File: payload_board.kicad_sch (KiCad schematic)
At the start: 93 parts, among them IC1 RP2040_QFN56, IC2 AZ1117CH-3.3TRG1, J1 Cam_PicoLock, J11 Stemma, J12 5025700893, J15 Debug_Conn, J2 Cam_Conn, J3 Antenna_Conn, J4 usb jumper, J5 Display_Conn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

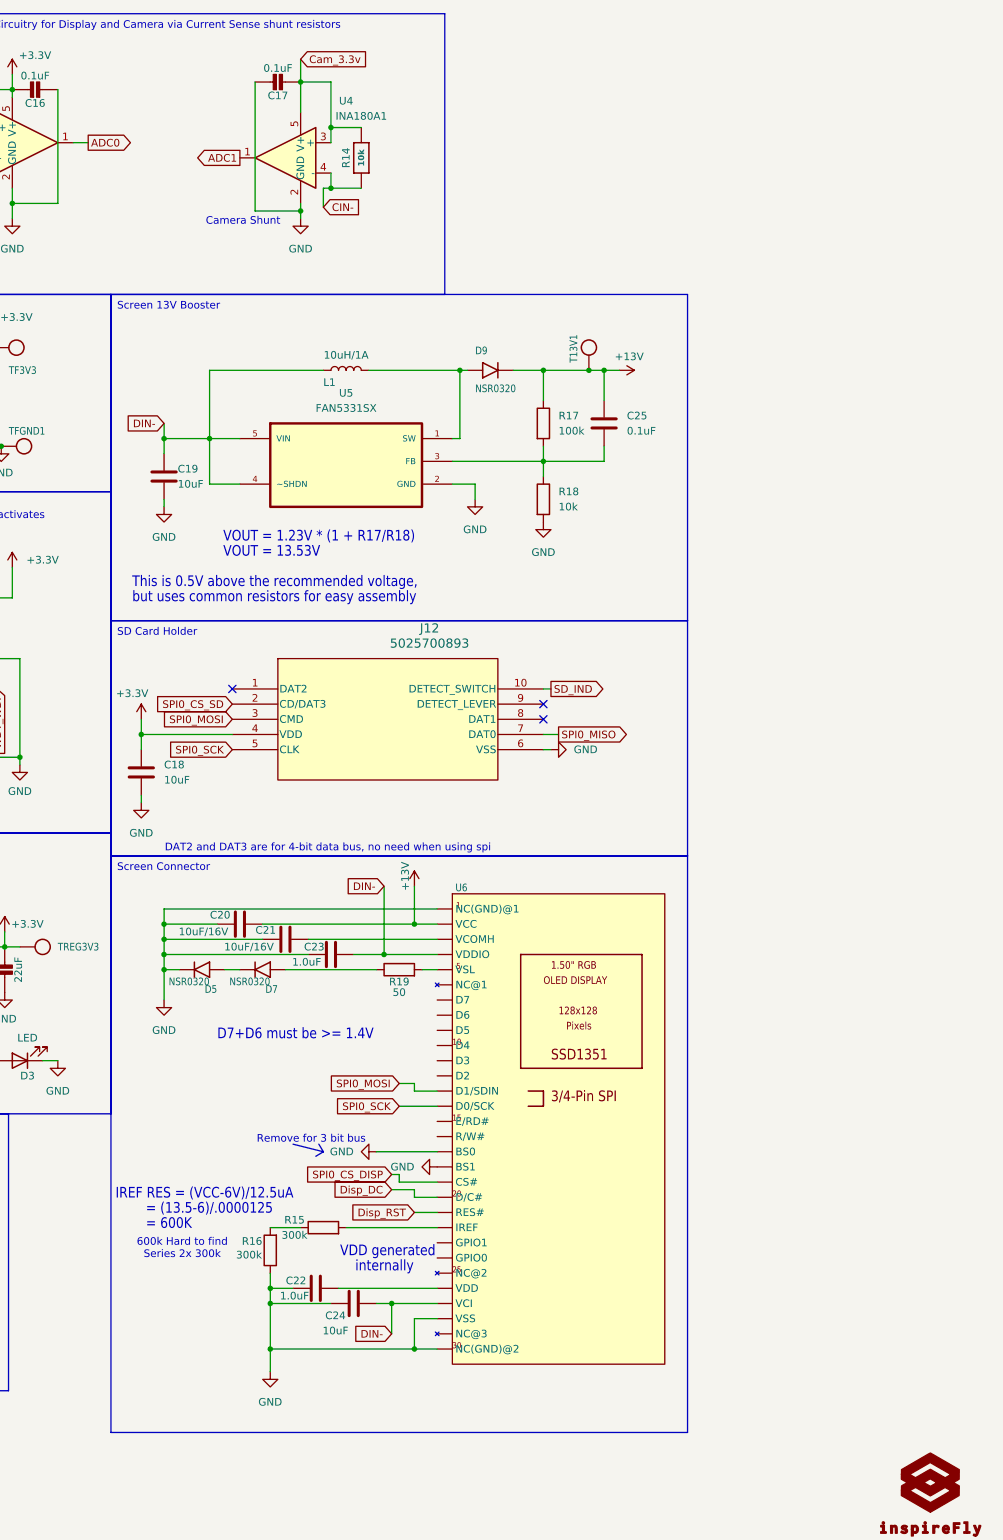
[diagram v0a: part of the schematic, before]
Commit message: Fixed RP2040 connections and changed sd card
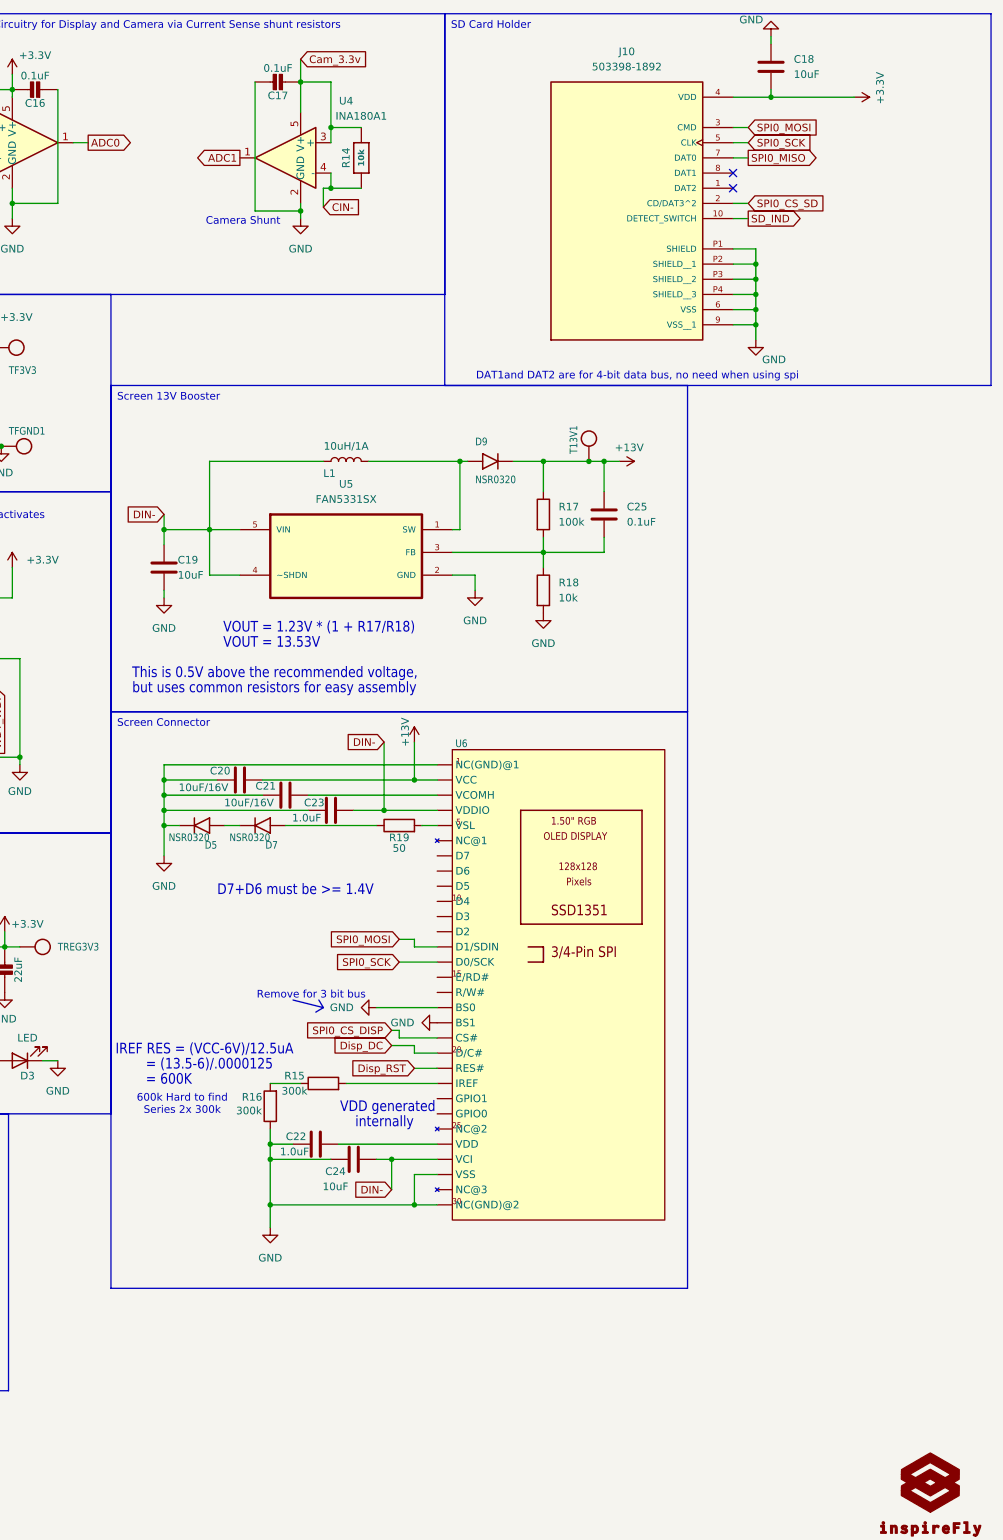
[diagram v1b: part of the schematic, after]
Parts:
- removed J12: 5025700893, PayloadBoard:502570-0893_MOL, symbol PayloadBoard:5025700893
- added J10: 503398-1892, PayloadBoard:MOLEX_503398-1892, symbol PayloadBoard:503398-1892
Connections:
- net +3.3V: now also C18.2, J10.4 (VDD); no longer C18.1
- net GND: now also C18.1, J10.6 (VSS), J10.9 (VSS__1), J10.P1 (SHIELD), J10.P2 (SHIELD__1), J10.P3 (SHIELD__2), J10.P4 (SHIELD__3); no longer C18.2
- net SD_IND: now also J10.10 (DETECT_SWITCH)
- net SPI0_CS_SD: now also J10.2 (CD/DAT3^2)
- net SPI0_MISO: now also J10.7 (DAT0)
- net SPI0_MOSI: now also J10.3 (CMD)
- net SPI0_SCK: now also J10.5 (CLK)
- no-connect marks 9 -> 8
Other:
- note added: "DAT1and DAT2 are for 4-bit data bus, no need when using spi"
- note removed: "DAT2 and DAT3 are for 4-bit data bus, no need when using spi"
- moved on the sheet: C18, C19, C20, C21, C22, C23, C24, C25, D5, D7, D9, L1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

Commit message: Changed some components to decrease bom count (C18, C25)
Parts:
- C18: footprint Capacitor_SMD:C_0603_1608Metric_Pad1.08x0.95mm_HandSolder -> Capacitor_SMD:C_1206_3216Metric_Pad1.33x1.80mm_HandSolder
- C25: footprint Capacitor_SMD:C_0603_1608Metric_Pad1.08x0.95mm_HandSolder -> Capacitor_SMD:C_0402_1005Metric_Pad0.74x0.62mm_HandSolder
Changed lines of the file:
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@@
 			)
 		)
-		(property "Footprint" "Capacitor_SMD:C_0603_1608Metric_Pad1.08x0.95mm_HandSolder"
+		(property "Footprint" "Capacitor_SMD:C_0402_1005Metric_Pad0.74x0.62mm_HandSolder"
 			(at 343.8652 100.33 0)
 			(effects
@@
 			)
 		)
-		(property "Footprint" "Capacitor_SMD:C_0603_1608Metric_Pad1.08x0.95mm_HandSolder"
+		(property "Footprint" "Capacitor_SMD:C_1206_3216Metric_Pad1.33x1.80mm_HandSolder"
 			(at 371.8052 25.4 0)
 			(effects

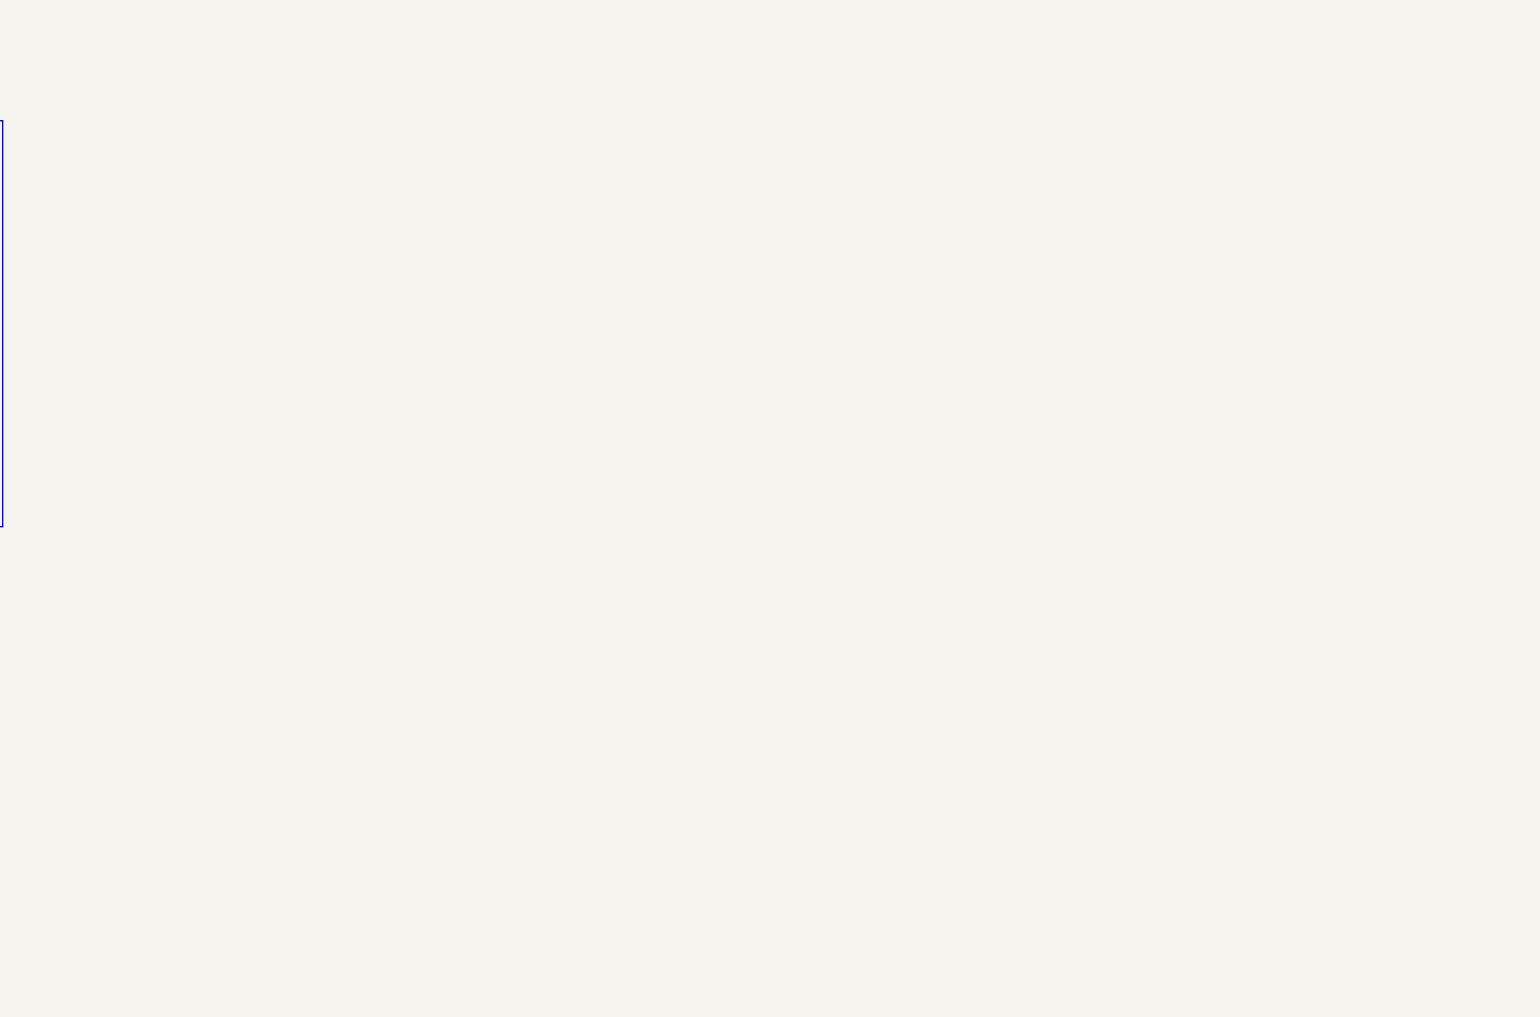
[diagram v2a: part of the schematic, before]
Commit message: stuck with new buck converter Trying to understand why BOOT is limited to 10 V, even if output is supposed to be 14V
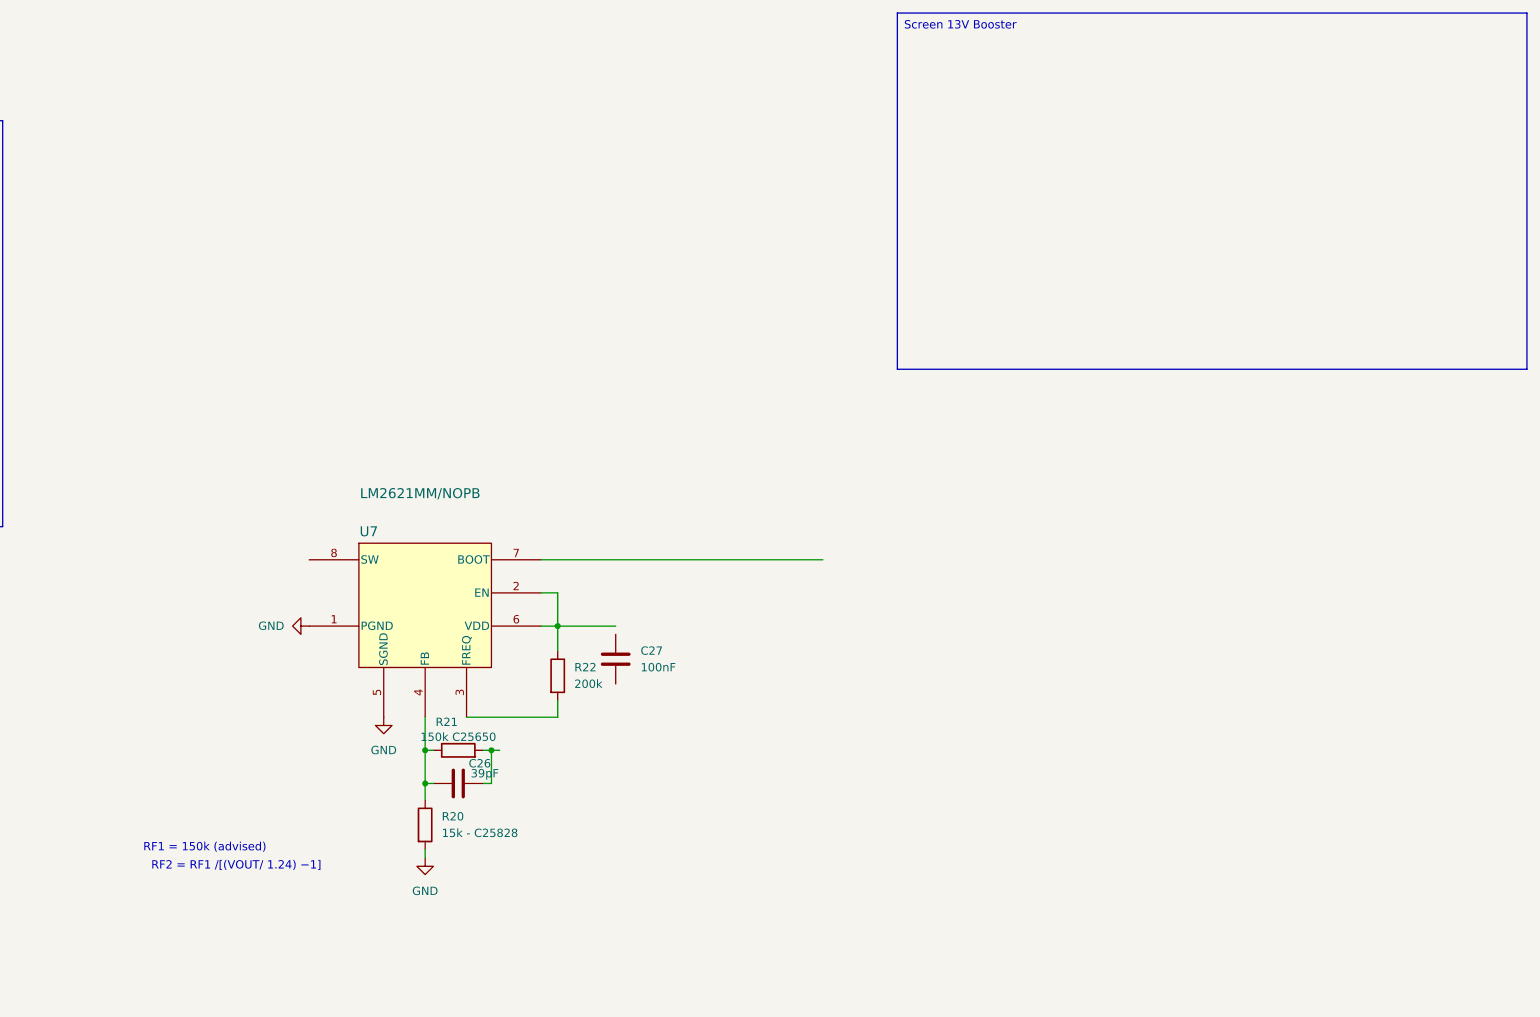
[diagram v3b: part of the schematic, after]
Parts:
- added C26: 39pF, symbol Device:C
- added C27: 100nF, symbol Device:C
- added R20: 15k - C25828, symbol Device:R
- added R21: 150k C25650, symbol Device:R
- added R22: 200k, symbol Device:R
- added U7: LM2621MM/NOPB, PayloadBoard:MUA08A, symbol PayloadBoard:LM2621MM_NOPB
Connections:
- net GND: now also R20.2, U7.1 (PGND), U7.5 (SGND)
- new net: C26.2, R20.1, R21.1, U7.4 (FB)
- new net: C26.1, R21.2
- new net: R22.1, U7.2 (EN), U7.6 (VDD)
- new net: R22.2, U7.3 (FREQ)
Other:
- note added: "RF1 = 150k (advised)"
- note added: "RF2 = RF1 /[(VOUT/ 1.24) −1]"

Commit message: Added new 13V boost converter
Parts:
- removed C25: 0.1uF, Capacitor_SMD:C_0402_1005Metric_Pad0.74x0.62mm_HandSolder, symbol Device:C
- removed C27: 100nF, symbol Device:C
- removed D9: NSR0320, Diode_SMD:D_SOD-323, symbol Adafruit ItsyBitsy RP2040-eagle-import:DIODESOD-323F
- removed R17: 100k, Resistor_SMD:R_0603_1608Metric_Pad0.98x0.95mm_HandSolder, symbol Device:R
- removed R18: 10k, Resistor_SMD:R_0603_1608Metric_Pad0.98x0.95mm_HandSolder, symbol Device:R
- removed R22: 200k, symbol Device:R
- removed U5: FAN5331SX, Package_TO_SOT_SMD:SOT-23-5_HandSoldering, symbol PayloadBoard:FAN5331SX
- removed U7: LM2621MM/NOPB, PayloadBoard:MUA08A, symbol PayloadBoard:LM2621MM_NOPB
- added U7: TLV61046ADB, Package_TO_SOT_SMD:SOT-23-6, symbol Regulator_Switching:TLV61046ADB
- C19: value 10uF -> 1uF; footprint Capacitor_SMD:C_0603_1608Metric_Pad1.08x0.95mm_HandSolder -> Capacitor_SMD:C_0402_1005Metric_Pad0.74x0.62mm_HandSolder
- C26: value 39pF -> 4.7uF; footprint (none) -> Resistor_SMD:R_0805_2012Metric_Pad1.20x1.40mm_HandSolder
- R20: value 15k - C25828 -> 16k; footprint (none) -> Resistor_SMD:R_0805_2012Metric_Pad1.20x1.40mm_HandSolder
- R21: value 150k C25650 -> 1k; footprint (none) -> Resistor_SMD:R_0402_1005Metric_Pad0.72x0.64mm_HandSolder
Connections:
- net +13V: now also C26.2, R20.1, U7.5 (VOUT)
- net DIN-: now also C19.2, U7.4 (EN), U7.6 (VI); no longer C19.1
- net GND: now also C19.1, C26.1, R21.2, U7.2 (GND); no longer C19.2, R20.2
- net at L1.2: now also U7.1 (SW)
- new net: R20.2, R21.1, U7.3 (FB)
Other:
- note added: "16k = (13.515/0.795-1)1k"
- note added: "R20 = (VOUT/0.795-1)R21"
- note removed: "RF1 = 150k (advised)"
- note removed: "RF2 = RF1 /[(VOUT/ 1.24) −1]"
- note removed: "VOUT = 1.23V * (1 + R17/R18)"
- note removed: "VOUT = 13.53V"
- moved on the sheet: C19, L1, T13V1

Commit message: Change part selection to reflect avaliability
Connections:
- net GND: now also IC1.40 (GPIO28/AD2), IC1.41 (GPIO29/AD3)
- no-connect marks 8 -> 7
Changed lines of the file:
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@@
 	)
 	(junction
+		(at 54.61 114.3)
+		(diameter 0)
+		(color 0 0 0 0)
+	)
+	(junction
 		(at 368.3 54.61)
 		(diameter 0)
@@
 	)
 	(no_connect
-		(at 54.61 113.03)
-	)
-	(no_connect
 		(at 209.55 220.98)
 	)
@@
 	)
 	(no_connect
-		(at 54.61 115.57)
+		(at 54.61 102.87)
 	)
 	(no_connect
-		(at 54.61 102.87)
+		(at 130.81 123.19)
 	)
 	(no_connect
@@
 	(wire
 		(pts
+			(xy 54.61 114.3) (xy 54.61 113.03)
+		)
+		(stroke
+			(width 0)
+			(type default)
+		)
+	)
+	(wire
+		(pts
 			(xy 140.97 177.8) (xy 148.59 177.8)
 		)
@@
 	(wire
 		(pts
+			(xy 54.61 114.3) (xy 54.61 115.57)
+		)
+		(stroke
+			(width 0)
+			(type default)
+		)
+	)
+	(wire
+		(pts
 			(xy 203.2 120.65) (xy 203.2 118.11)
 		)
@@
 	(wire
 		(pts
+			(xy 45.72 114.3) (xy 54.61 114.3)
+		)
+		(stroke
+			(width 0)
+			(type default)
+		)
+	)
+	(wire
+		(pts
 			(xy 364.49 57.15) (xy 368.3 57.15)
 		)
@@
 					(unit 1)
 				)
+			)
+		)
+	)
+	(symbol
+		(lib_name "GND_1")
+		(lib_id "power:GND")
+		(at 45.72 114.3 0)
+		(unit 1)
+		(exclude_from_sim no)
+		(in_bom yes)
+		(on_board yes)
+		(dnp no)
+		(property "Reference" "#PWR060"
+			(at 45.72 120.65 0)
+			(effects
+				(font
+					(size 1.27 1.27)
+				)
+				(hide yes)
+			)
+		)
+		(property "Value" "GND"
+			(at 41.91 115.824 0)
+			(effects
+				(font
+					(size 1.27 1.27)
+				)
+			)
+		)
+		(property "Footprint" ""
+			(at 45.72 114.3 0)
+			(effects
+				(font
+					(size 1.27 1.27)
+				)
+				(hide yes)
+			)
+		)
+		(property "Datasheet" ""
+			(at 45.72 114.3 0)
+			(effects
+				(font
+					(size 1.27 1.27)
+				)
+				(hide yes)
+			)
+		)
+		(property "Description" "Power symbol creates a global label with name \"GND\" , ground"
+			(at 45.72 114.3 0)
+			(effects
+				(font
+					(size 1.27 1.27)
+				)
+				(hide yes)
+			)
+		)
+		(pin "1"
+		)
+		(instances
+			(project ""
+				(path "/e3f40ef2-c677-4aae-b100-4b87fee46bc8"
+					(reference "#PWR060")
+					(unit 1)
+				)

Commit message: Added alternative 13v regulator setup for testing
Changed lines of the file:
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@@
-	)
-	(junction
-		(at 27.94 93.98)
-		(diameter 0)
-		(color 0 0 0 0)
 	)
 	(junction
@@
 		)
 		(stroke
-			(width 0)
-			(type default)
-		)
-	)
-	(wire
-		(pts
-			(xy 26.67 93.98) (xy 27.94 93.98)
-		)
-		(stroke
